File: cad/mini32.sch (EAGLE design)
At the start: 54 parts, among them CN1 MICROSDPLAIN, J1 HEADER-5X1, Q1 MOSFETSOT-23, Q2 MOSFET-P, SW2 SWITCHKMR211, SW3 SWITCHKMR211, U1 STM32F411/48, U2 MPU-9150, U3 MCP73831/OT, U4 MCP1824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

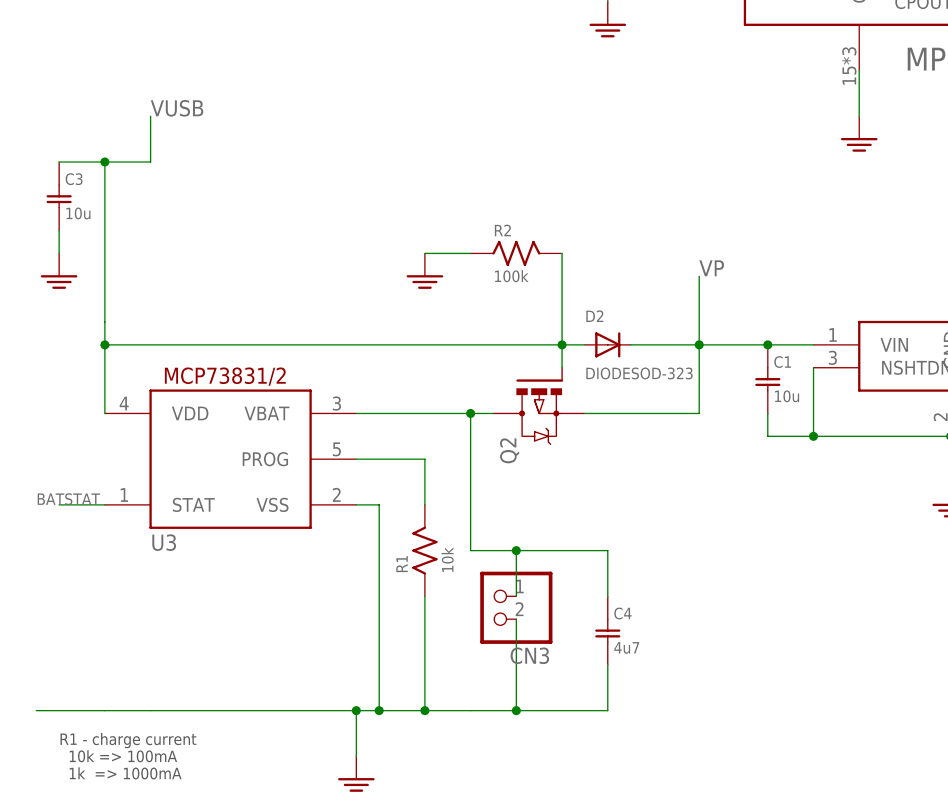
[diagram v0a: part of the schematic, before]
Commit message: replace charger
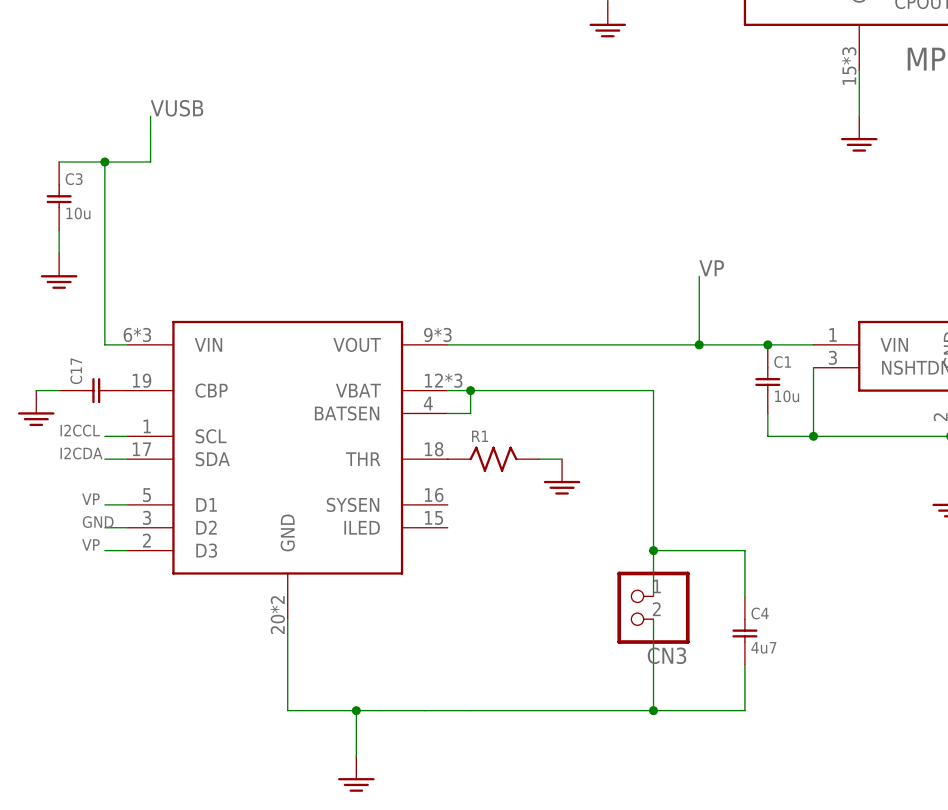
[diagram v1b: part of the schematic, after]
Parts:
- removed D2: DIODESOD-323, jaw:DIODESOD-323
- removed Q2: MOSFET-P, jaw:MOSFET-P
- removed R2: 100k, jaw:R0603
- added C17: (no value), jaw:C0603
- R1: value 10k -> (none)
- U3: value MCP73831/OT -> ADP5062; device adafruit:MCP73831/OT -> jaw:ADP5062
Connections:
- removed net N$1: R1.P$2, U3.PROG
- new net N$5: C17.P$2, U3.CBP
- new net N$6: R1.P$1, U3.THR
- net BATSTAT: no longer U3.STAT
- net GND: now also C17.P$1, R1.P$2, U3.D2, U3.GND; no longer R1.P$1, R2.P$1, U3.VSS
- net I2CCL: now also U3.SCL
- net I2CDA: now also U3.SDA
- net VBAT: now also U3.BATSEN; no longer Q2.D
- net VP: now also U3.D1, U3.D3, U3.VOUT; no longer D2.C, Q2.S
- net VUSB: now also U3.VIN; no longer D2.A, Q2.G, R2.P$2, U3.VDD
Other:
- note removed: "R1 - charge current 10k => 100mA 1k => 1000mA"
- moved on the sheet: C4, CN3, R1

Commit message: ok
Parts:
- removed C6, C7: (no value), jaw:C0603
- removed U$1: (no value), adafruit:CR2032SMT
- added B1: BATTERY-CR2016, jaw:BATTERY-CR2016
- added U$4: ROBOTMAN-LOGO, jaw:ROBOTMAN-LOGO
- C12: value (none) -> 0.1u
- C13: value (none) -> 2.2n
- C14: value (none) -> .1u
- C17: value (none) -> 10n
- C8, C9: value (none) -> 5p
- R1: value (none) -> 10k
- R8: value (none) -> 470
- X1: value XTAL32X15 -> 12MHz; device jaw:XTAL32X15 -> jaw:RESONATORCTCE
- X2: value XTAL32X15 -> 32k768
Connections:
- removed net N$29: U1.PB4
- new net IMUINT: U1.PB4, U2.INT
- net BATSTAT: now also U3.SYSEN
- net GND: now also B1.M, X1.G; no longer C6.P$1, C7.P$1, U$1.+1
- net N$12: now also X1.X1; no longer C6.P$2, X1.P$1
- net N$13: now also X1.X2; no longer C7.P$2, X1.P$2
- net N$21: now also B1.P; no longer U$1.-
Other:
- moved on the sheet: C12, C13, C23

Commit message: lsm303d
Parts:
- C12: value 0.1u -> 4.7u
- C13: value 2.2n -> .22u
- U2: value MPU-9150 -> LSM303D; device jaw:MPU-9150 -> jaw:LSM303D
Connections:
- new net N$1: C12.P$1, U2.C1
- net GND: now also U2.SA0; no longer C13.P$2, U2.AD0, U2.CLKIN, U2.FSYNC
- net IMUINT: now also U2.INT1; no longer U2.INT
- net N$2: now also C13.P$2, U2.SETP; no longer C12.P$1, U2.REGOUT
- net N$4: now also U2.SETC; no longer U2.CPOUT
- net VCC: now also U2.CS, U2.VDD, U2.VDDIO; no longer U2.VCC, U2.VLOGIC
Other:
- moved on the sheet: C12, C13, C14
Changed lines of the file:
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@@
 <part name="U$2" library="adafruit" deviceset="FIDUCIAL" device=""/>
 <part name="U$3" library="adafruit" deviceset="FIDUCIAL" device=""/>
-<part name="U2" library="jaw" deviceset="MPU-9150" device=""/>
-<part name="C12" library="jaw" deviceset="C" device="0603" value="0.1u"/>
-<part name="C13" library="jaw" deviceset="C" device="0603" value="2.2n"/>
+<part name="C12" library="jaw" deviceset="C" device="0603" value="4.7u"/>
+<part name="C13" library="jaw" deviceset="C" device="0603" value=".22u"/>
 <part name="C14" library="jaw" deviceset="C" device="0603" value=".1u"/>
 <part name="GND12" library="jaw" deviceset="PWR-GND" device=""/>
 <part name="GND14" library="jaw" deviceset="PWR-GND" device=""/>
-<part name="GND15" library="jaw" deviceset="PWR-GND" device=""/>
 <part name="VCC4" library="jaw" deviceset="PWR-VCC" device=""/>
 <part name="GND19" library="jaw" deviceset="PWR-GND" device=""/>
@@
 <part name="B1" library="jaw" deviceset="BATTERY" device="-CR2016"/>
 <part name="X1" library="jaw" deviceset="RESONATOR" device="CTCE" value="12MHz"/>
+<part name="U2" library="jaw" deviceset="LSM303D" device=""/>
 </parts>
 <sheets>
@@
 <instance part="U$2" gate="G$1" x="269.24" y="40.64"/>
 <instance part="U$3" gate="G$1" x="261.62" y="40.64"/>
-<instance part="U2" gate="G$1" x="99.06" y="106.68"/>
-<instance part="C12" gate="G$1" x="129.54" y="101.6" rot="R90"/>
-<instance part="C13" gate="G$1" x="129.54" y="96.52" rot="R90"/>
-<instance part="C14" gate="G$1" x="124.46" y="119.38"/>
+<instance part="C12" gate="G$1" x="127" y="109.22" rot="R90"/>
+<instance part="C13" gate="G$1" x="124.46" y="101.6" rot="R90"/>
+<instance part="C14" gate="G$1" x="132.08" y="119.38"/>
 <instance part="GND12" gate="G$1" x="99.06" y="81.28"/>
-<instance part="GND14" gate="G$1" x="137.16" y="86.36"/>
-<instance part="GND15" gate="G$1" x="71.12" y="93.98"/>
+<instance part="GND14" gate="G$1" x="132.08" y="86.36"/>
 <instance part="VCC4" gate="G$1" x="99.06" y="132.08"/>
 <instance part="GND19" gate="G$1" x="30.48" y="167.64"/>
@@
 <instance part="B1" gate="G$1" x="226.06" y="170.18"/>
 <instance part="X1" gate="G$1" x="144.78" y="160.02"/>
+<instance part="U2" gate="G$1" x="99.06" y="106.68"/>
 </instances>
 <busses>
@@
 </segment>
 <segment>
+<pinref part="GND12" gate="G$1" pin="GND"/>
+<wire x1="99.06" y1="88.9" x2="99.06" y2="86.36" width="0.1524" layer="91"/>
 <pinref part="U2" gate="G$1" pin="GND"/>
-<pinref part="GND12" gate="G$1" pin="GND"/>
-<wire x1="99.06" y1="88.9" x2="99.06" y2="83.82" width="0.1524" layer="91"/>
+<wire x1="99.06" y1="86.36" x2="99.06" y2="83.82" width="0.1524" layer="91"/>
+<junction x="99.06" y="86.36"/>
 </segment>
 <segment>
 <pinref part="C12" gate="G$1" pin="P$2"/>
-<wire x1="132.08" y1="101.6" x2="137.16" y2="101.6" width="0.1524" layer="91"/>
-<wire x1="137.16" y1="101.6" x2="137.16" y2="96.52" width="0.1524" layer="91"/>
-<pinref part="C13" gate="G$1" pin="P$2"/>
-<wire x1="137.16" y1="96.52" x2="132.08" y2="96.52" width="0.1524" layer="91"/>
+<wire x1="129.54" y1="109.22" x2="132.08" y2="109.22" width="0.1524" layer="91"/>
+<wire x1="132.08" y1="109.22" x2="132.08" y2="96.52" width="0.1524" layer="91"/>
 <pinref part="GND14" gate="G$1" pin="GND"/>
-<wire x1="137.16" y1="96.52" x2="137.16" y2="88.9" width="0.1524" layer="91"/>
-<junction x="137.16" y="96.52"/>
-<pinref part="U2" gate="G$1" pin="FSYNC"/>
-<wire x1="116.84" y1="114.3" x2="124.46" y2="114.3" width="0.1524" layer="91"/>
-<wire x1="124.46" y1="114.3" x2="137.16" y2="114.3" width="0.1524" layer="91"/>
-<wire x1="137.16" y1="114.3" x2="137.16" y2="101.6" width="0.1524" layer="91"/>
-<junction x="137.16" y="101.6"/>
+<wire x1="132.08" y1="96.52" x2="132.08" y2="88.9" width="0.1524" layer="91"/>
+<wire x1="132.08" y1="114.3" x2="132.08" y2="109.22" width="0.1524" layer="91"/>
+<junction x="132.08" y="109.22"/>
 <pinref part="C14" gate="G$1" pin="P$2"/>
-<wire x1="124.46" y1="116.84" x2="124.46" y2="114.3" width="0.1524" layer="91"/>
-<junction x="124.46" y="114.3"/>
-</segment>
-<segment>
-<pinref part="U2" gate="G$1" pin="AD0"/>
-<pinref part="GND15" gate="G$1" pin="GND"/>
-<wire x1="81.28" y1="101.6" x2="71.12" y2="101.6" width="0.1524" layer="91"/>
-<wire x1="71.12" y1="101.6" x2="71.12" y2="96.52" width="0.1524" layer="91"/>
-<pinref part="U2" gate="G$1" pin="CLKIN"/>
-<wire x1="81.28" y1="114.3" x2="71.12" y2="114.3" width="0.1524" layer="91"/>
-<wire x1="71.12" y1="114.3" x2="71.12" y2="101.6" width="0.1524" layer="91"/>
-<junction x="71.12" y="101.6"/>
+<wire x1="132.08" y1="116.84" x2="132.08" y2="114.3" width="0.1524" layer="91"/>
 </segment>
 <segment>
@@
 <wire x1="17.78" y1="38.1" x2="15.24" y2="38.1" width="0.1524" layer="91"/>
 <label x="12.7" y="38.1" size="1.27" layer="95"/>
+</segment>
+<segment>
+<pinref part="U2" gate="G$1" pin="SA0"/>
+<wire x1="81.28" y1="96.52" x2="76.2" y2="96.52" width="0.1524" layer="91"/>
+<label x="73.66" y="96.52" size="1.27" layer="95"/>
 </segment>
 </net>
@@
 <segment>
 <pinref part="C14" gate="G$1" pin="P$1"/>
-<wire x1="124.46" y1="124.46" x2="124.46" y2="127" width="0.1524" layer="91"/>
-<pinref part="U2" gate="G$1" pin="VLOGIC"/>
-<wire x1="124.46" y1="127" x2="101.6" y2="127" width="0.1524" layer="91"/>
+<wire x1="132.08" y1="124.46" x2="132.08" y2="127" width="0.1524" layer="91"/>
+<wire x1="132.08" y1="127" x2="101.6" y2="127" width="0.1524" layer="91"/>
 <wire x1="101.6" y1="127" x2="101.6" y2="124.46" width="0.1524" layer="91"/>
-<pinref part="U2" gate="G$1" pin="VCC"/>
 <wire x1="101.6" y1="127" x2="99.06" y2="127" width="0.1524" layer="91"/>
 <wire x1="99.06" y1="127" x2="96.52" y2="127" width="0.1524" layer="91"/>
@@
 <wire x1="99.06" y1="129.54" x2="99.06" y2="127" width="0.1524" layer="91"/>
 <junction x="99.06" y="127"/>
+<pinref part="U2" gate="G$1" pin="VDDIO"/>
+<junction x="96.52" y="127"/>
+<pinref part="U2" gate="G$1" pin="VDD"/>
 </segment>
 <segment>
@@
 <label x="246.38" y="177.8" size="1.27" layer="95"/>
 <pinref part="J1" gate="G$1" pin="1"/>
+</segment>
+<segment>
+<pinref part="U2" gate="G$1" pin="CS"/>
+<wire x1="81.28" y1="116.84" x2="76.2" y2="116.84" width="0.1524" layer="91"/>
+<label x="73.66" y="116.84" size="1.27" layer="95"/>
 </segment>
 </net>
@@
 </segment>
 </net>
-<net name="N$2" class="0">
-<segment>
-<pinref part="U2" gate="G$1" pin="REGOUT"/>
-<pinref part="C12" gate="G$1" pin="P$1"/>
-<wire x1="116.84" y1="101.6" x2="124.46" y2="101.6" width="0.1524" layer="91"/>
-</segment>
-</net>
-<net name="N$4" class="0">
-<segment>
-<pinref part="U2" gate="G$1" pin="CPOUT"/>
-<pinref part="C13" gate="G$1" pin="P$1"/>
-<wire x1="116.84" y1="96.52" x2="124.46" y2="96.52" width="0.1524" layer="91"/>
-</segment>
-</net>
 <net name="I2CCL" class="0">
-<segment>
-<pinref part="U2" gate="G$1" pin="SCL"/>
-<wire x1="81.28" y1="109.22" x2="78.74" y2="109.22" width="0.1524" layer="91"/>
-<label x="73.66" y="109.22" size="1.27" layer="95"/>
-</segment>
 <segment>
 <pinref part="U1" gate="G$1" pin="PB6"/>
@@
 <label x="10.16" y="48.26" size="1.27" layer="95"/>
 </segment>
+<segment>
+<pinref part="U2" gate="G$1" pin="SCL"/>
+<wire x1="81.28" y1="111.76" x2="76.2" y2="111.76" width="0.1524" layer="91"/>
+<label x="73.66" y="111.76" size="1.27" layer="95"/>
+</segment>
 </net>
 <net name="I2CDA" class="0">
-<segment>
-<pinref part="U2" gate="G$1" pin="SDA"/>
-<wire x1="81.28" y1="106.68" x2="78.74" y2="106.68" width="0.1524" layer="91"/>
-<label x="73.66" y="106.68" size="1.27" layer="95"/>
-</segment>
 <segment>
 <pinref part="U1" gate="G$1" pin="PB7"/>
@@
 <label x="10.16" y="45.72" size="1.27" layer="95"/>
 </segment>
+<segment>
+<pinref part="U2" gate="G$1" pin="SDA"/>
+<wire x1="81.28" y1="109.22" x2="76.2" y2="109.22" width="0.1524" layer="91"/>
+<label x="73.66" y="109.22" size="1.27" layer="95"/>
+</segment>
 </net>
 <net name="DPYDC" class="0">
@@
 </segment>
 <segment>
-<pinref part="U2" gate="G$1" pin="INT"/>
-<wire x1="116.84" y1="99.06" x2="119.38" y2="99.06" width="0.1524" layer="91"/>
-<label x="119.38" y="99.06" size="1.27" layer="95"/>
+<pinref part="U2" gate="G$1" pin="INT1"/>
+<wire x1="81.28" y1="101.6" x2="76.2" y2="101.6" width="0.1524" layer="91"/>
+<label x="73.66" y="101.6" size="1.27" layer="95"/>
 </segment>
 </net>
@@
 </segment>
 </net>
+<net name="N$1" class="0">
+<segment>
+<pinref part="C12" gate="G$1" pin="P$1"/>
+<pinref part="U2" gate="G$1" pin="C1"/>
+<wire x1="121.92" y1="109.22" x2="114.3" y2="109.22" width="0.1524" layer="91"/>
+</segment>
+</net>
+<net name="N$2" class="0">
+<segment>
+<pinref part="U2" gate="G$1" pin="SETP"/>
+<wire x1="114.3" y1="106.68" x2="127" y2="106.68" width="0.1524" layer="91"/>
+<pinref part="C13" gate="G$1" pin="P$2"/>
+<wire x1="127" y1="106.68" x2="127" y2="101.6" width="0.1524" layer="91"/>
+</segment>
+</net>
+<net name="N$4" class="0">
+<segment>
+<pinref part="C13" gate="G$1" pin="P$1"/>
+<wire x1="119.38" y1="101.6" x2="116.84" y2="101.6" width="0.1524" layer="91"/>
+<wire x1="116.84" y1="101.6" x2="116.84" y2="104.14" width="0.1524" layer="91"/>
+<pinref part="U2" gate="G$1" pin="SETC"/>
+<wire x1="116.84" y1="104.14" x2="114.3" y2="104.14" width="0.1524" layer="91"/>
+</segment>
+</net>

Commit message: max17048
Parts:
- added U5: MAX17048, jaw:MAX17048
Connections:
- new net N$22: U5.ALERT
- net GND: now also U5.CTG, U5.GND, U5.QSTRT
- net I2CCL: now also U5.SCL
- net I2CDA: now also U5.SDA
- net VBAT: now also U5.VCC
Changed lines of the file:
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@@
 <part name="X1" library="jaw" deviceset="RESONATOR" device="CTCE" value="12MHz"/>
 <part name="U2" library="jaw" deviceset="LSM303D" device=""/>
+<part name="U5" library="jaw" deviceset="MAX17048" device=""/>
 </parts>
 <sheets>
@@
 <instance part="X1" gate="G$1" x="144.78" y="160.02"/>
 <instance part="U2" gate="G$1" x="99.06" y="106.68"/>
+<instance part="U5" gate="G$1" x="127" y="25.4"/>
 </instances>
 <busses>
@@
 <pinref part="U3" gate="G$1" pin="GND"/>
 <wire x1="35.56" y1="27.94" x2="35.56" y2="17.78" width="0.1524" layer="91"/>
+<pinref part="U5" gate="G$1" pin="CTG"/>
+<wire x1="111.76" y1="22.86" x2="99.06" y2="22.86" width="0.1524" layer="91"/>
+<wire x1="99.06" y1="22.86" x2="99.06" y2="20.32" width="0.1524" layer="91"/>
+<wire x1="99.06" y1="20.32" x2="99.06" y2="17.78" width="0.1524" layer="91"/>
+<wire x1="99.06" y1="17.78" x2="86.36" y2="17.78" width="0.1524" layer="91"/>
+<junction x="86.36" y="17.78"/>
+<pinref part="U5" gate="G$1" pin="GND"/>
+<wire x1="111.76" y1="20.32" x2="99.06" y2="20.32" width="0.1524" layer="91"/>
+<junction x="99.06" y="20.32"/>
 </segment>
 <segment>
@@
 <label x="73.66" y="96.52" size="1.27" layer="95"/>
 </segment>
+<segment>
+<pinref part="U5" gate="G$1" pin="QSTRT"/>
+<wire x1="142.24" y1="22.86" x2="147.32" y2="22.86" width="0.1524" layer="91"/>
+<label x="147.32" y="22.86" size="1.27" layer="95"/>
+</segment>
 </net>
 <net name="VCC" class="0">
@@
 <wire x1="55.88" y1="50.8" x2="55.88" y2="53.34" width="0.1524" layer="91"/>
 <junction x="55.88" y="53.34"/>
+<pinref part="U5" gate="G$1" pin="VCC"/>
+<wire x1="111.76" y1="27.94" x2="99.06" y2="27.94" width="0.1524" layer="91"/>
+<wire x1="99.06" y1="27.94" x2="99.06" y2="35.56" width="0.1524" layer="91"/>
+<wire x1="99.06" y1="35.56" x2="86.36" y2="35.56" width="0.1524" layer="91"/>
+<junction x="86.36" y="35.56"/>
 </segment>
 </net>
@@
 <label x="73.66" y="111.76" size="1.27" layer="95"/>
 </segment>
+<segment>
+<pinref part="U5" gate="G$1" pin="SCL"/>
+<wire x1="142.24" y1="27.94" x2="147.32" y2="27.94" width="0.1524" layer="91"/>
+<label x="147.32" y="27.94" size="1.27" layer="95"/>
+</segment>
 </net>
 <net name="I2CDA" class="0">
@@
 <wire x1="81.28" y1="109.22" x2="76.2" y2="109.22" width="0.1524" layer="91"/>
 <label x="73.66" y="109.22" size="1.27" layer="95"/>
+</segment>
+<segment>
+<pinref part="U5" gate="G$1" pin="SDA"/>
+<wire x1="142.24" y1="30.48" x2="147.32" y2="30.48" width="0.1524" layer="91"/>
+<label x="147.32" y="30.48" size="1.27" layer="95"/>
 </segment>
 </net>
@@
 </segment>
 </net>
+<net name="N$22" class="0">
+<segment>
+<pinref part="U5" gate="G$1" pin="ALERT"/>
+<wire x1="142.24" y1="20.32" x2="147.32" y2="20.32" width="0.1524" layer="91"/>
+</segment>
+</net>

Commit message: embiggen connectors
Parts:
- removed CN6: (no value), jaw:HEADER-2X4
- added CONN1: HEADER-5X2-PTH, jaw:HEADER-5X2-PTH
- added LOGO1: OSHW-LOGOM, Sparkfun-Aesthetics:OSHW-LOGOM
- added U$1: ROBOTMAN-LOGO, jaw:ROBOTMAN-LOGO
- JP1: value (none) -> HEADER-21X1; device adafruit:PINHD-1X20 -> jaw:HEADER-21X1
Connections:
- net BOOT0: now also JP1.15
- net DPYCS: now also CONN1.7; no longer CN6.P$7
- net DPYDC: now also CONN1.6; no longer CN6.P$6
- net GND: now also CONN1.8; no longer CN6.P$8
- net I2CCL: now also CONN1.9, JP1.17; no longer JP1.15
- net I2CDA: now also CONN1.10, JP1.18; no longer JP1.16
- net NRST: now also CONN1.2, JP1.16; no longer CN6.P$2, JP1.17
- net SPIMISO: now also CONN1.3, JP1.21; no longer CN6.P$3, JP1.20
- net SPIMOSI: now also CONN1.5, JP1.20; no longer CN6.P$5, JP1.19
- net SPISCK: now also CONN1.4, JP1.19; no longer CN6.P$4, JP1.18
- net VCC: now also CONN1.1; no longer CN6.P$1
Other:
- note added: "display"
- note removed: "M471-OLED display"

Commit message: tweak
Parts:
- added R2: 100, jaw:R0603
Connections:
- new net N$9: Q1.G, R2.P$2
- net IOB9: now also R2.P$1; no longer Q1.G
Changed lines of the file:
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@@
 <part name="LOGO1" library="Sparkfun-Aesthetics" deviceset="OSHW-LOGO" device="M"/>
 <part name="U$1" library="jaw" deviceset="ROBOTMAN-LOGO" device=""/>
+<part name="R2" library="jaw" deviceset="R" device="0603" value="100"/>
 </parts>
 <sheets>
@@
 <instance part="LOGO1" gate="G$1" x="203.2" y="45.72"/>
 <instance part="U$1" gate="G$1" x="238.76" y="40.64"/>
+<instance part="R2" gate="G$1" x="17.78" y="121.92"/>
 </instances>
 <busses>
@@
 <net name="IOB9" class="0">
 <segment>
-<pinref part="Q1" gate="G$1" pin="G"/>
-<wire x1="22.86" y1="121.92" x2="17.78" y2="121.92" width="0.1524" layer="91"/>
-<label x="12.7" y="121.92" size="1.27" layer="95"/>
-</segment>
-<segment>
 <pinref part="U1" gate="G$1" pin="PB9"/>
 <wire x1="193.04" y1="116.84" x2="198.12" y2="116.84" width="0.1524" layer="91"/>
 <label x="198.12" y="116.84" size="1.27" layer="95"/>
+</segment>
+<segment>
+<pinref part="R2" gate="G$1" pin="P$1"/>
+<wire x1="10.16" y1="121.92" x2="12.7" y2="121.92" width="0.1524" layer="91"/>
+<label x="7.62" y="121.92" size="1.27" layer="95"/>
 </segment>
 </net>
@@
 </segment>
 </net>
+<net name="N$9" class="0">
+<segment>
+<pinref part="Q1" gate="G$1" pin="G"/>
+<pinref part="R2" gate="G$1" pin="P$2"/>
+</segment>
+</net>
